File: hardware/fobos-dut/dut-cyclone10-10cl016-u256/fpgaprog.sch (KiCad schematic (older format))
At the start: 8 parts, among them J7 0878321420, SW1 SW_DIP_x03, U1 10CL016YU256I7G

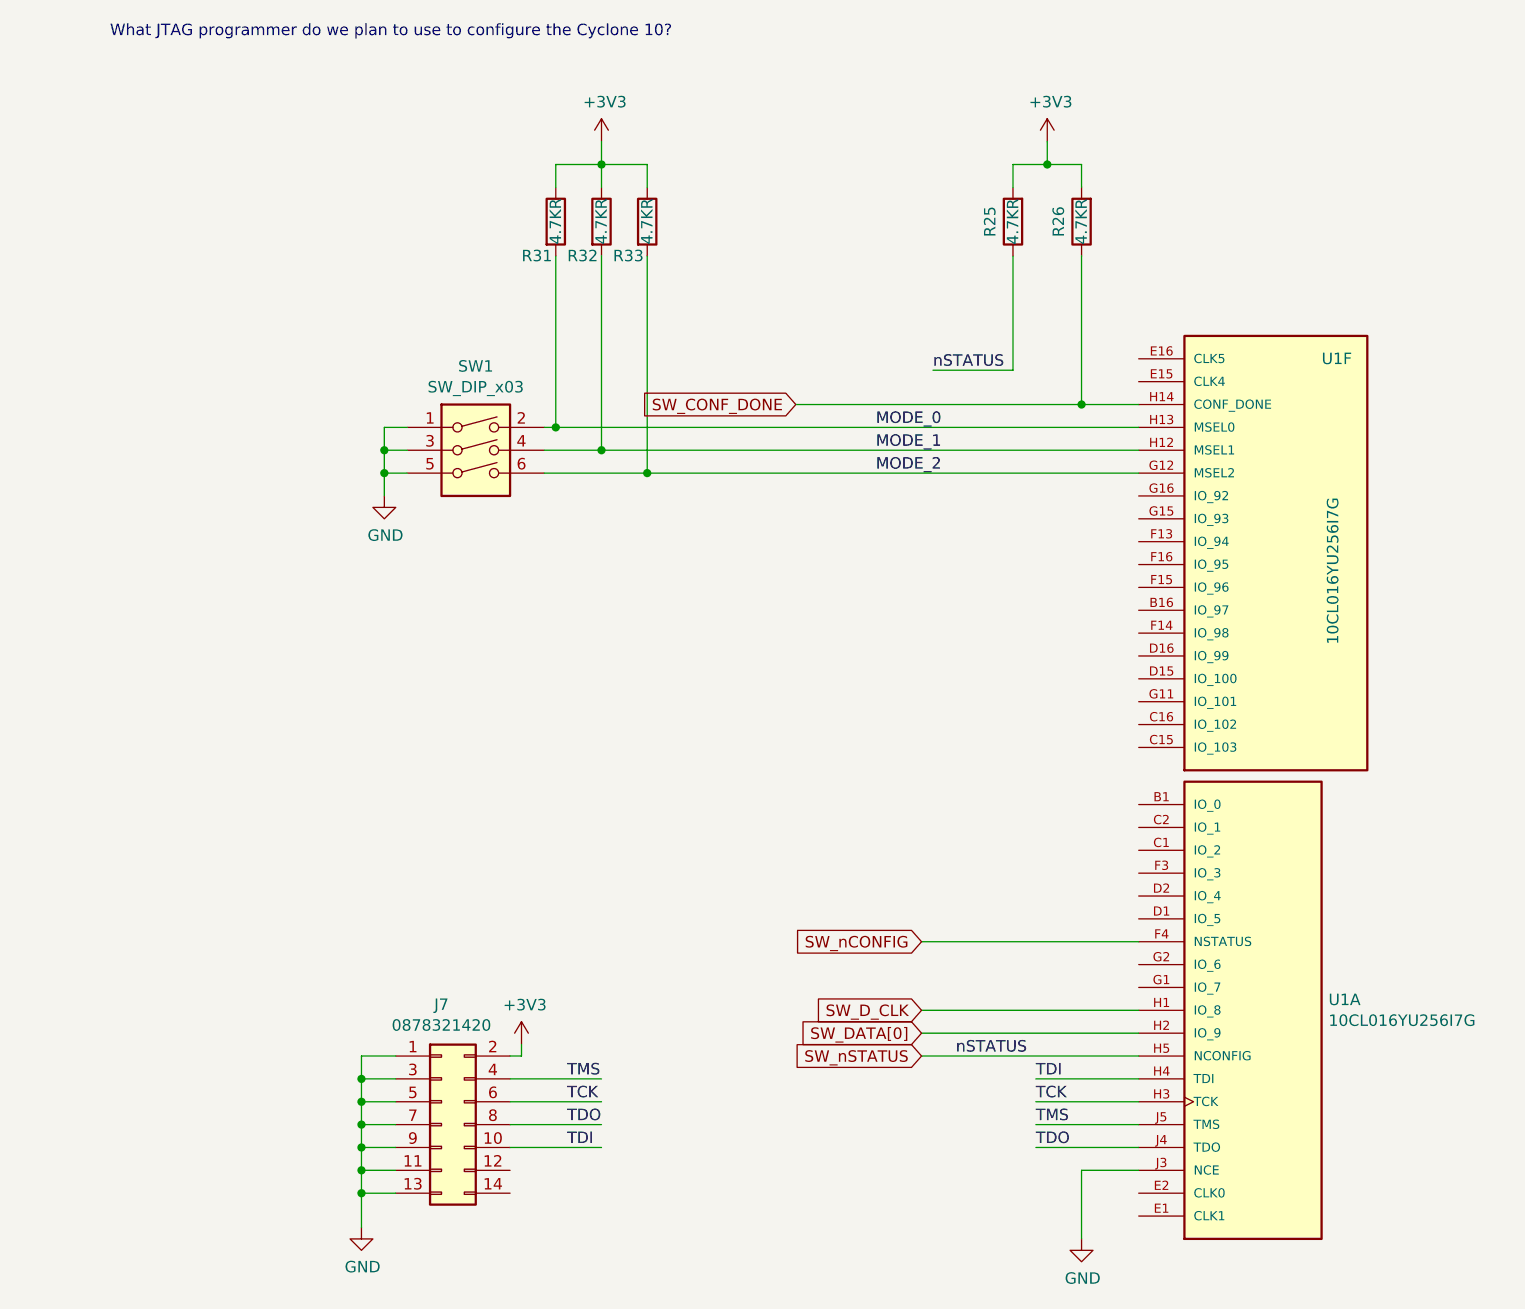
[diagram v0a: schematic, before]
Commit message: Updated jtag connector to match terasic usb blaster Connected SPI Flash Layout is in work
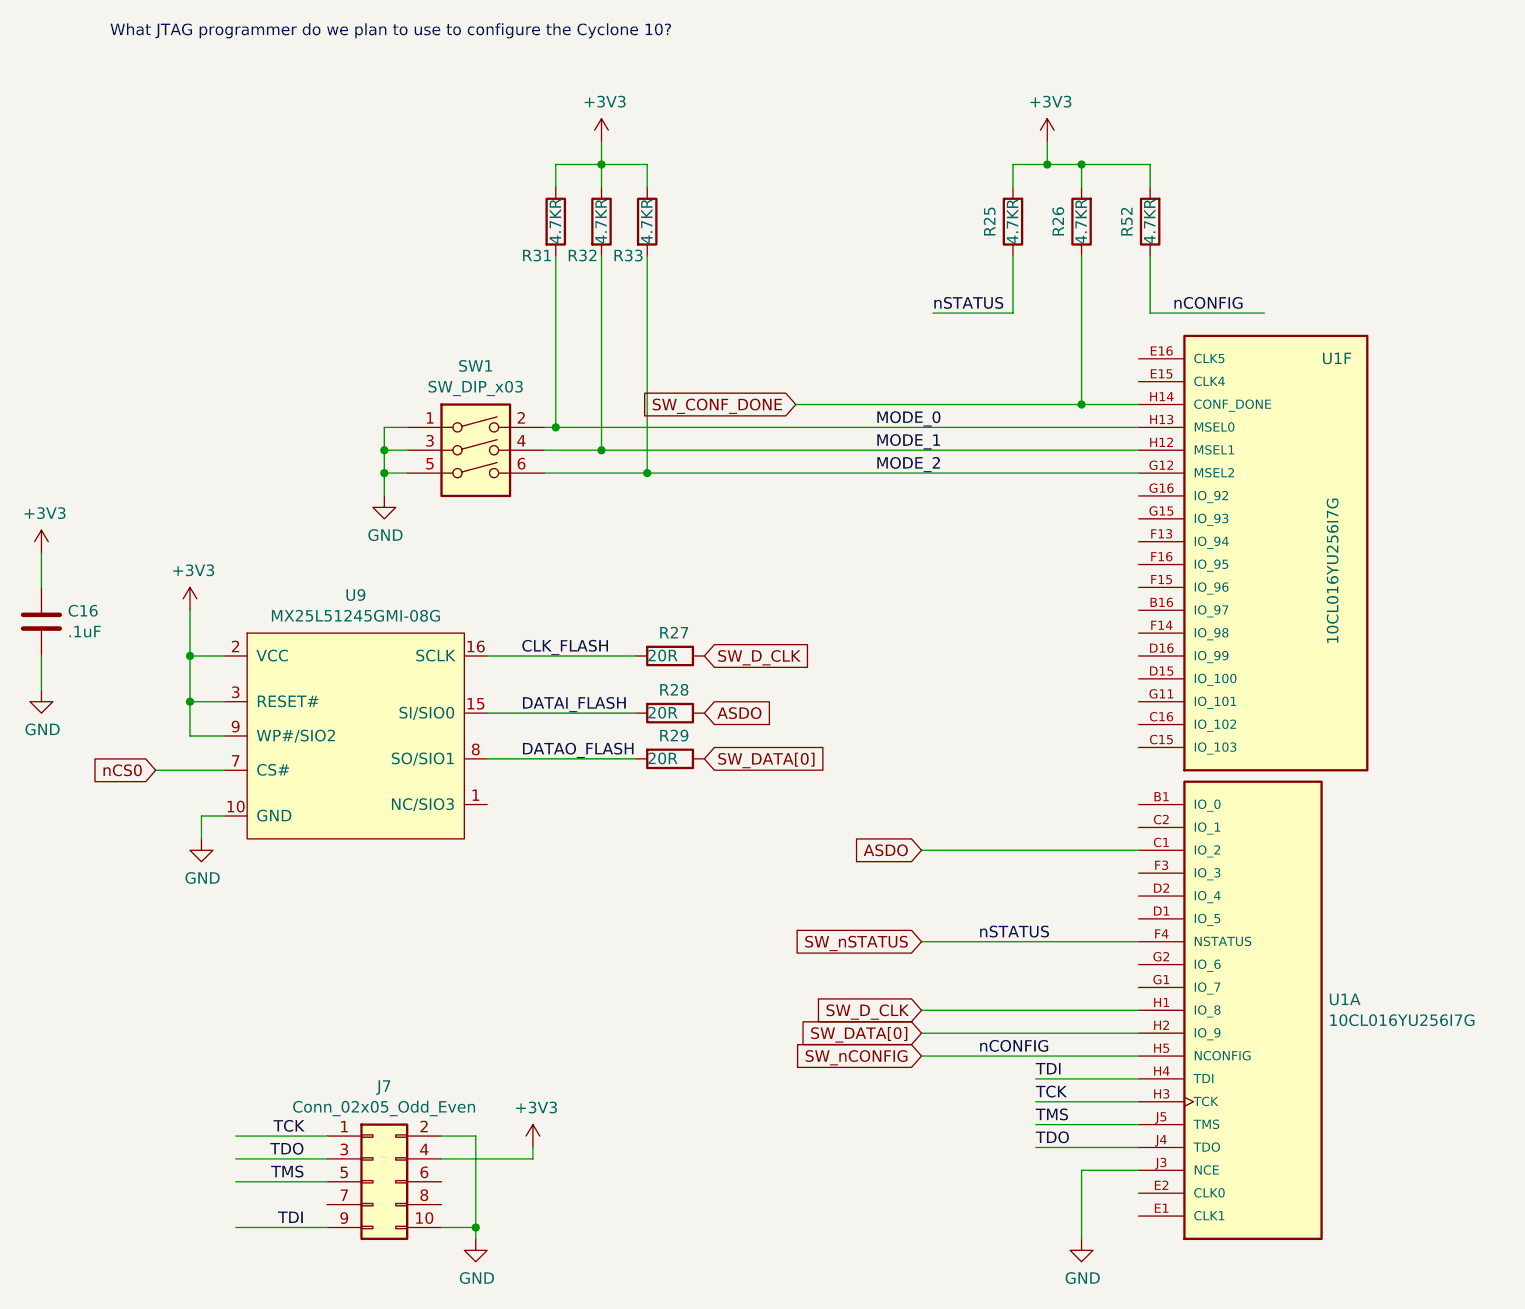
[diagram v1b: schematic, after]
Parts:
- removed J7: 0878321420, cerg:PinHeader_2x7_P2mm_SMD, symbol Connector_Generic:Conn_02x07_Odd_Even
- added C16: .1uF, Capacitor_SMD:C_0402_1005Metric_Pad0.74x0.62mm_HandSolder, symbol Device:C
- added J7: Conn_02x05_Odd_Even, Connector_PinHeader_2.54mm:PinHeader_2x05_P.54mm_Vertical_Shrouded, symbol Connector_Generic:Conn_02x05_Odd_Even
- added R27, R28, R29: 20R, Resistor_SMD:R_0603_1608Metric, symbol Device:R
- added R52: 4.7KR, Resistor_SMD:R_0603_1608Metric, symbol Device:R
- added U9: MX25L51245GMI-08G, Package_SO:SOIC-16W_7.5x10.3mm_P1.27mm, symbol cerg:MX25L51245GMI-08G
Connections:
- net labels added: ASDO, CLK_FLASH, DATAI_FLASH, DATAO_FLASH, nCONFIG, nCS0
- wire segments 61 -> 70
